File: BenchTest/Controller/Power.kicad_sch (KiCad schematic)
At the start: 1 part, among them J1 Conn_01x02

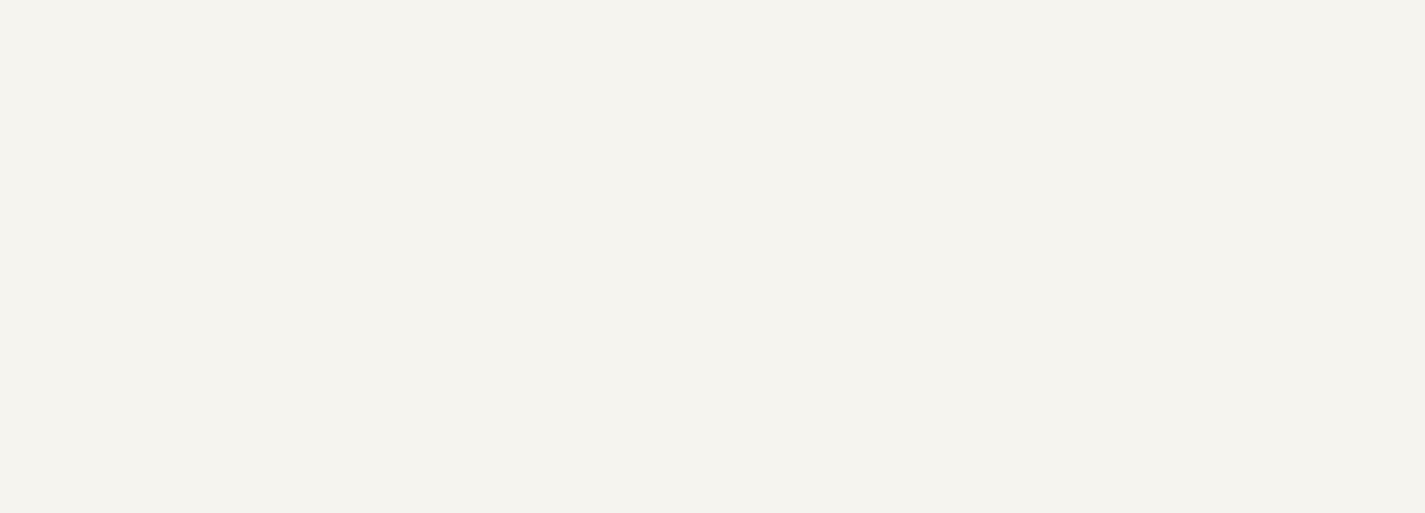
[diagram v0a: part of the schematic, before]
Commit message: Added Power Module for MCU
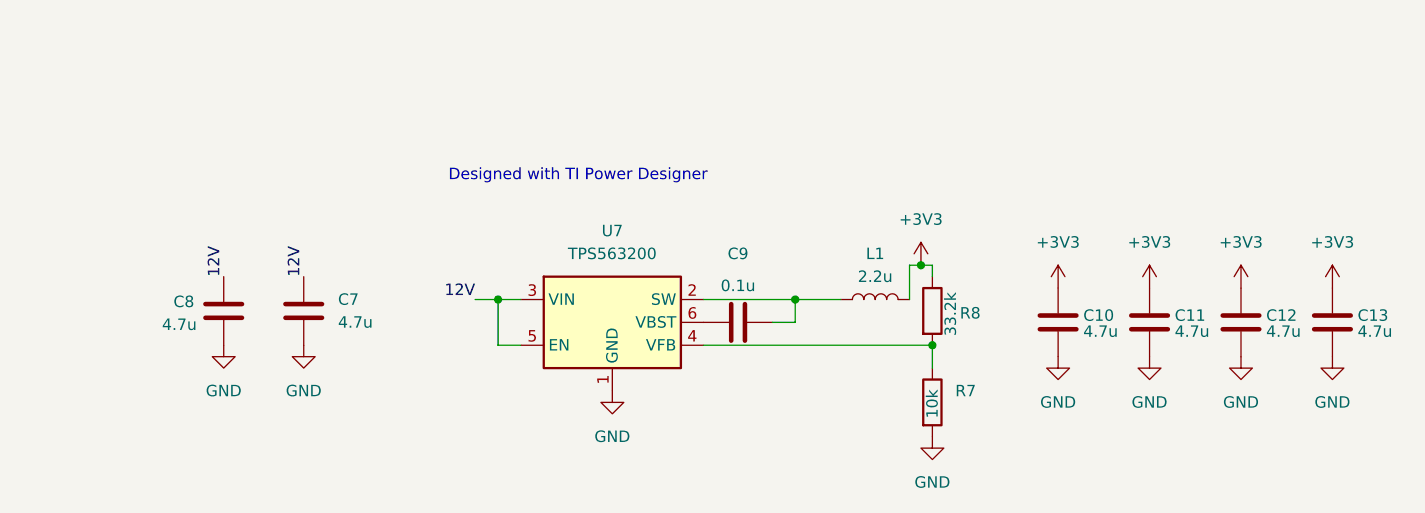
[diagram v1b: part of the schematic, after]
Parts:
- added C10, C11, C12, C13, C7, C8: 4.7u, Capacitor_SMD:C_0603_1608Metric_Pad1.08x0.95mm_HandSolder, symbol Device:C
- added C9: 0.1u, Capacitor_SMD:C_0402_1005Metric_Pad0.74x0.62mm_HandSolder, symbol Device:C
- added L1: 2.2u, Inductor_SMD:L_0805_2012Metric_Pad1.05x1.20mm_HandSolder, symbol Device:L
- added R7: 10k, Resistor_SMD:R_0201_0603Metric_Pad0.64x0.40mm_HandSolder, symbol Device:R
- added R8: 33.2k, Resistor_SMD:R_0201_0603Metric_Pad0.64x0.40mm_HandSolder, symbol Device:R
- added U7: TPS563200, Package_TO_SOT_SMD:SOT-23-6, symbol Regulator_Switching:TPS563200
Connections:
- net 12V: now also C7.1, C8.1, U7.3 (VIN), U7.5 (EN)
- net GND: now also C10.2, C11.2, C12.2, C13.2, C7.2, C8.2, R7.2, U7.1 (GND)
- new net: R7.1, R8.2, U7.4 (VFB)
- new net: C9.1, U7.6 (VBST)
- new net: C9.2, L1.1, U7.2 (SW)
- new net +3V3: C10.1, C11.1, C12.1, C13.1, L1.2, R8.1
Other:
- note added: "Designed with TI Power Designer"

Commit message: WIP Controller in progress
w
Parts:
- added C14, C15, C17, C18, C19, C20: 4.7u, Capacitor_SMD:C_0603_1608Metric_Pad1.08x0.95mm_HandSolder, symbol Device:C
- added C16: 0.1u, Capacitor_SMD:C_0402_1005Metric_Pad0.74x0.62mm_HandSolder, symbol Device:C
- added L2: 2.2u, Inductor_SMD:L_0805_2012Metric_Pad1.05x1.20mm_HandSolder, symbol Device:L
- added R10: 10k, Resistor_SMD:R_0201_0603Metric_Pad0.64x0.40mm_HandSolder, symbol Device:R
- added R9: 56.2k, Resistor_SMD:R_0201_0603Metric_Pad0.64x0.40mm_HandSolder, symbol Device:R
- added U8: TPS563200, Package_TO_SOT_SMD:SOT-23-6, symbol Regulator_Switching:TPS563200
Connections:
- net 12V: now also C14.1, C15.1, U8.3 (VIN), U8.5 (EN)
- net GND: now also C14.2, C15.2, C17.2, C18.2, C19.2, C20.2, R10.2, U8.1 (GND)
- new net: R10.1, R9.2, U8.4 (VFB)
- new net: C16.2, L2.1, U8.2 (SW)
- new net: C16.1, U8.6 (VBST)
- new net +5V: C17.1, C18.1, C19.1, C20.1, L2.2, R9.1
